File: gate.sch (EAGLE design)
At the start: 0 parts

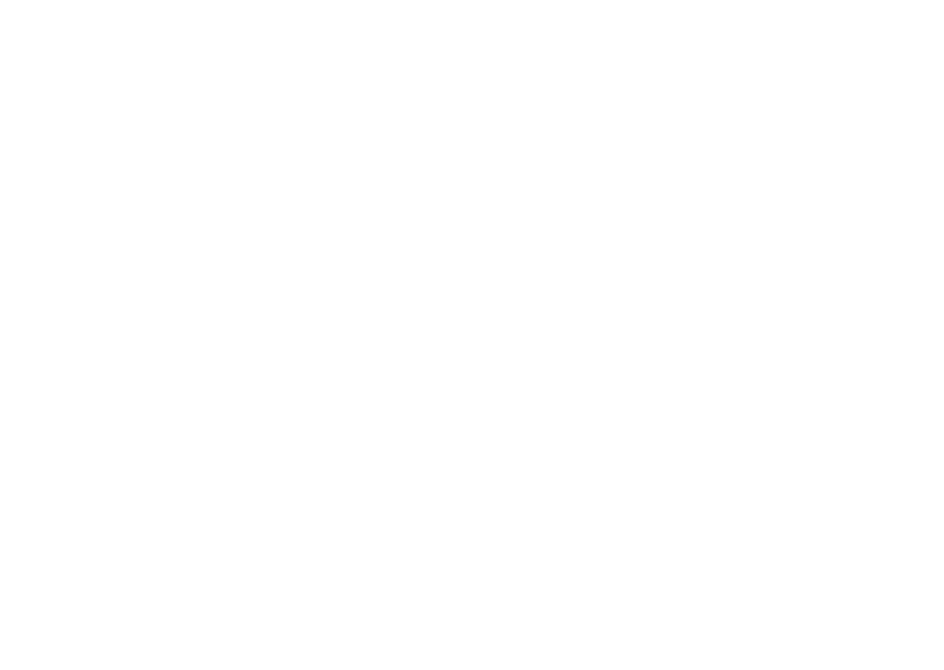
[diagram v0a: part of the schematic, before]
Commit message: Add RS-232 interface
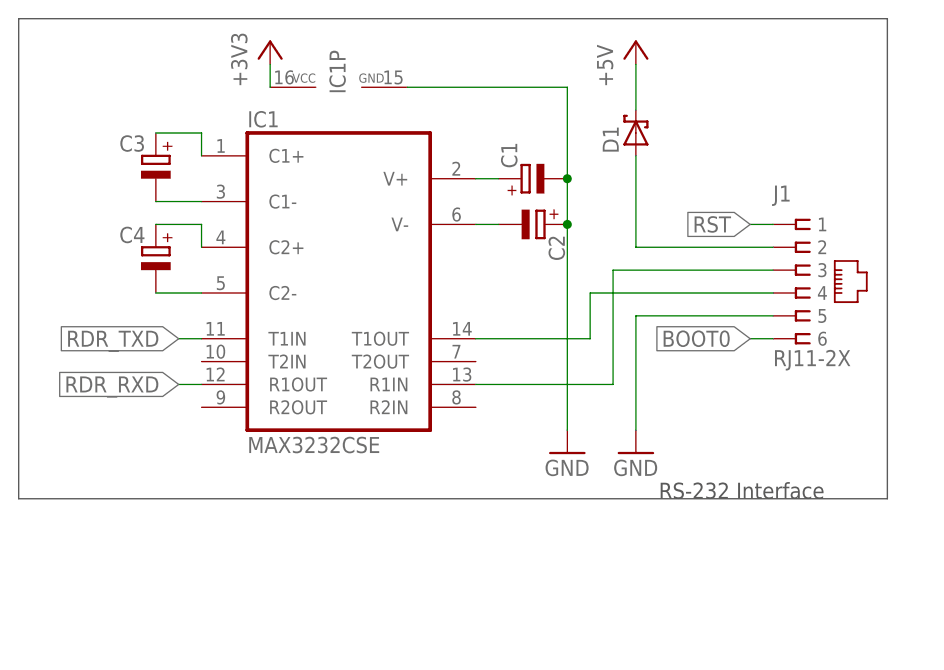
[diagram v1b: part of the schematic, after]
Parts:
- added C1, C2, C3, C4: (no value), rcl:CPOL-EU153CLV-0505
- added D1: (no value), diode:SCHOTTKY-DIODESMD
- added IC1: MAX3232CSE, maxim:MAX3232CSE
- added J1: RJ11-2X, con-tycoelectronics:RJ11-2X
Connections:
- new net +3V3: IC1P.VCC
- new net +5V: D1.C
- new net BOOT0: J1.6
- new net GND: C1.-, C2.+, IC1P.GND, J1.5
- new net N$1: IC1G$1.R1IN, J1.3
- new net N$2: IC1G$1.T1OUT, J1.4
- new net N$3: C3.+, IC1G$1.C1+
- new net N$4: C3.-, IC1G$1.C1-
- new net N$5: C4.+, IC1G$1.C2+
- new net N$6: C4.-, IC1G$1.C2-
- new net N$7: C1.+, IC1G$1.V+
- new net N$8: C2.-, IC1G$1.V-
- new net N$9: D1.A, J1.2
- new net RDR_RXD: IC1G$1.R1OUT
- new net RDR_TXD: IC1G$1.T1IN
- new net RST: J1.1
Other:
- note added: "RS-232 Interface"

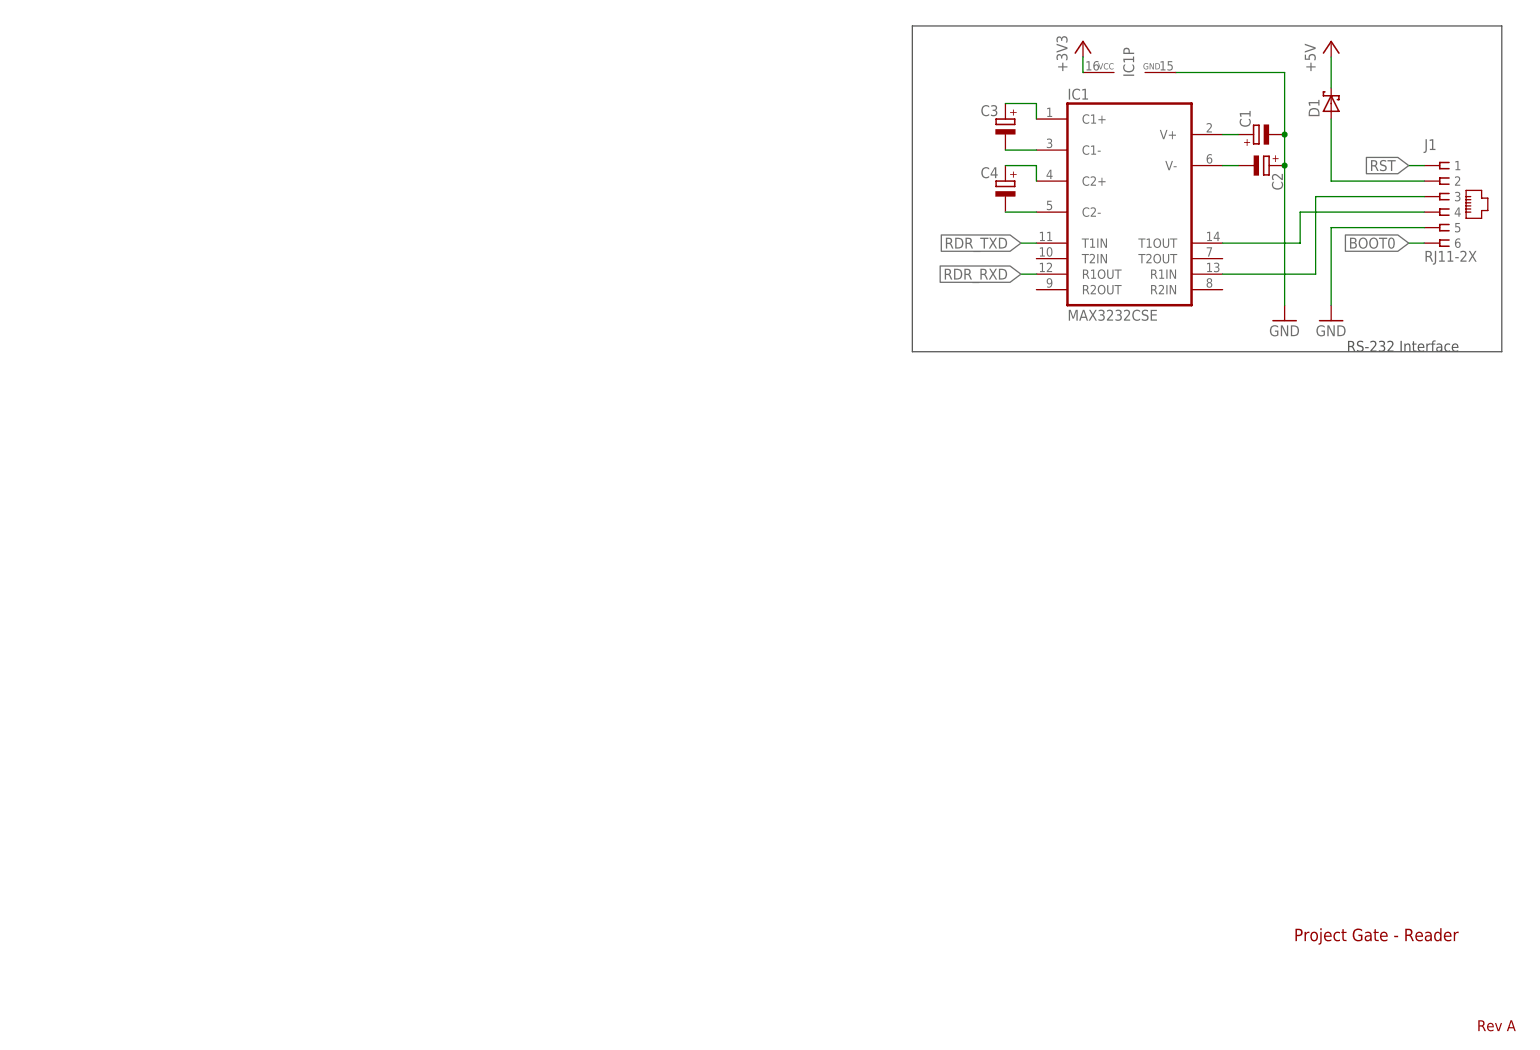
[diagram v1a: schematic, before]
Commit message: Add audio output
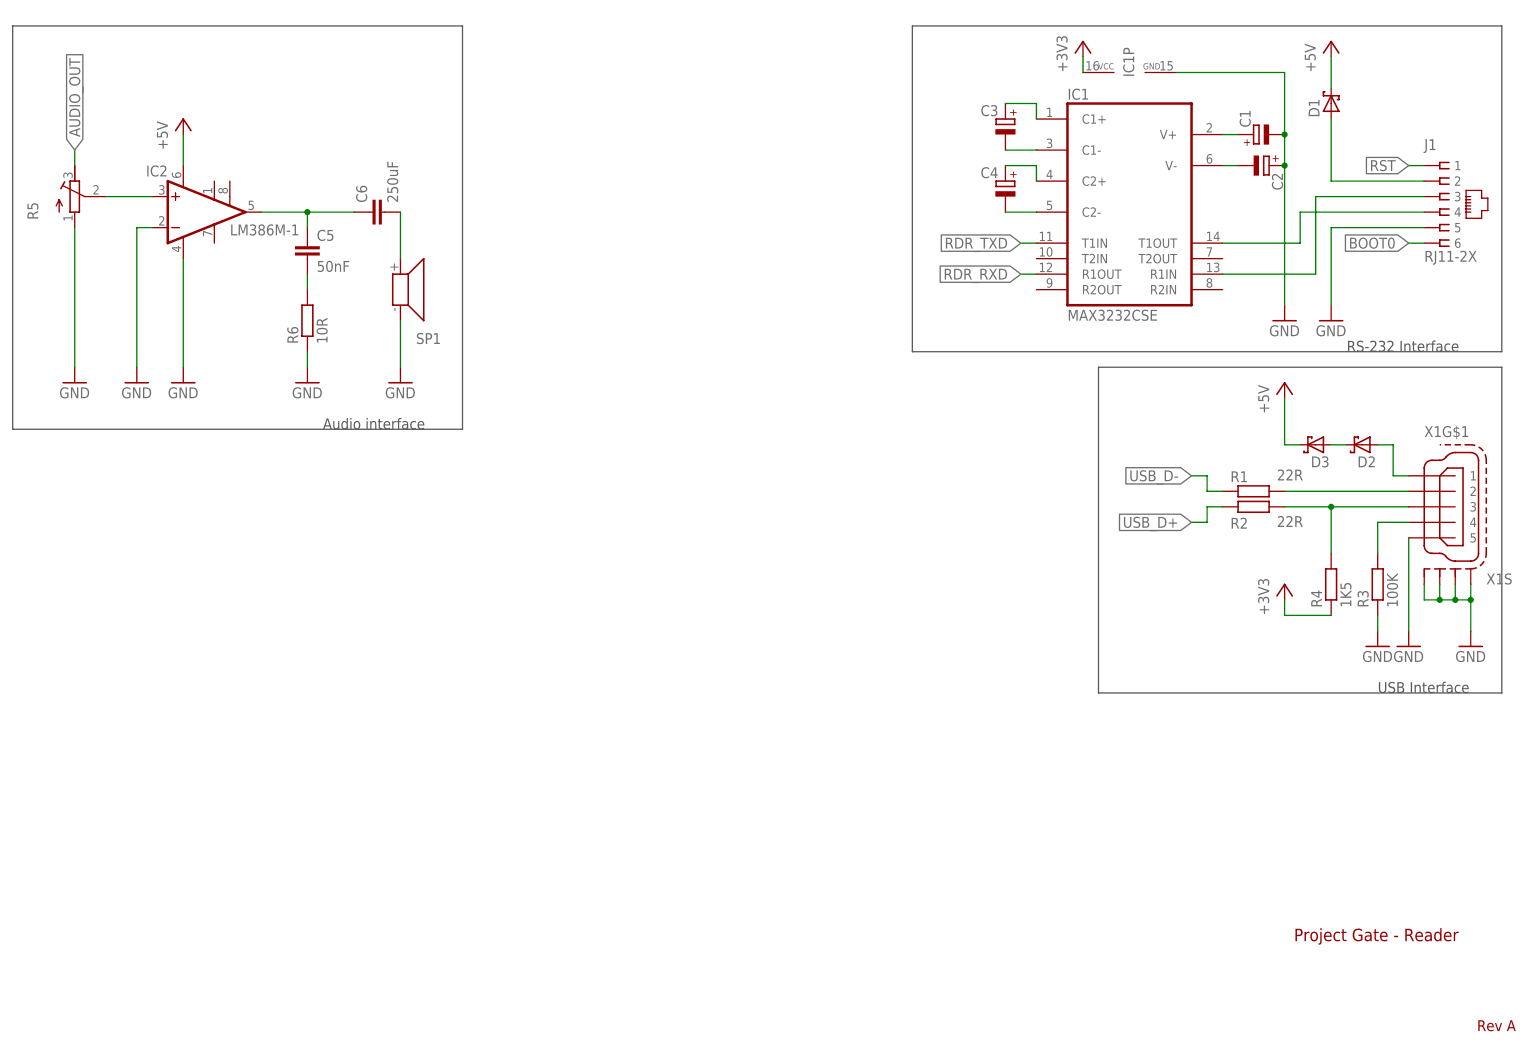
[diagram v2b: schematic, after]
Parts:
- added C5: 50nF, rcl:C-EUC0805
- added C6: 250uF, rcl:C-EUC0805
- added D2, D3: (no value), diode:SCHOTTKY-DIODESMD
- added IC2: LM386M-1, linear:LM386M-1
- added R1, R2: 22R, rcl:R-EU_R0805
- added R3: 100K, rcl:R-EU_R0805
- added R4: 1K5, rcl:R-EU_R0805
- added R5: (no value), rcl:R-TRIMM3339P
- added R6: 10R, rcl:R-EU_R0805
- added SP1: SMS-1308MS-2-R, speaker:SMS-1308MS-2-R
- added X1: MINI-USB-SCHIELD-32005-301, con-cypressindustries:MINI-USB-SCHIELD-32005-301
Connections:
- new net AUDIO_OUT: R5.E
- new net N$10: D2.C, D3.A
- new net N$11: D2.A, X1G$1.1
- new net N$12: R1.2, X1G$1.2
- new net N$13: R2.2, R4.2, X1G$1.3
- new net N$14: R3.2, X1G$1.4
- new net N$15: IC2.+IN, R5.S
- new net N$16: C5.1, C6.1, IC2.OUT
- new net N$17: C5.2, R6.2
- new net N$18: C6.2, SP1.1
- new net USB_D+: R2.1
- new net USB_D-: R1.1
- net +3V3: now also R4.1
- net +5V: now also D3.C, IC2.VS
- net GND: now also IC2.-IN, IC2.GND, R3.1, R5.A, R6.1, SP1.2, X1G$1.5, X1S.S1, X1S.S2, X1S.S3, X1S.S4
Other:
- note added: "Audio interface"
- note added: "USB Interface"

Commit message: Minor mid-review fixes
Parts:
- removed D3: (no value), diode:SCHOTTKY-DIODESMD
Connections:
- removed net N$10: D2.C, D3.A
- new net +12V: D1.C
- net +3V3: now also C1.-
- net +5V: now also D2.C; no longer D1.C, D3.C
- net GND: no longer C1.-
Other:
- moved on the sheet: C1, C2, C3, C4, D1, D2, IC1, IC1P, J1, R1, R2, R3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

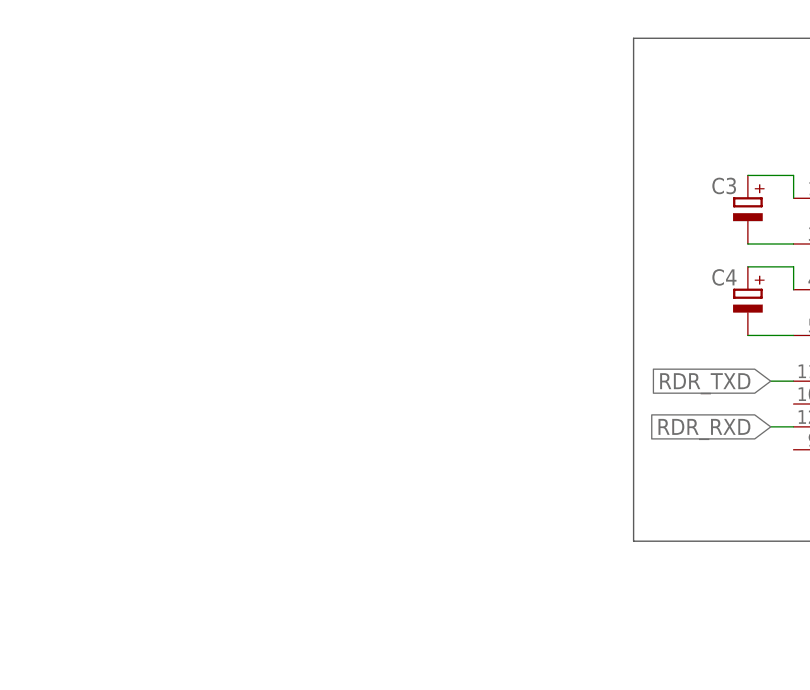
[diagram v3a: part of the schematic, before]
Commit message: Add LEDs
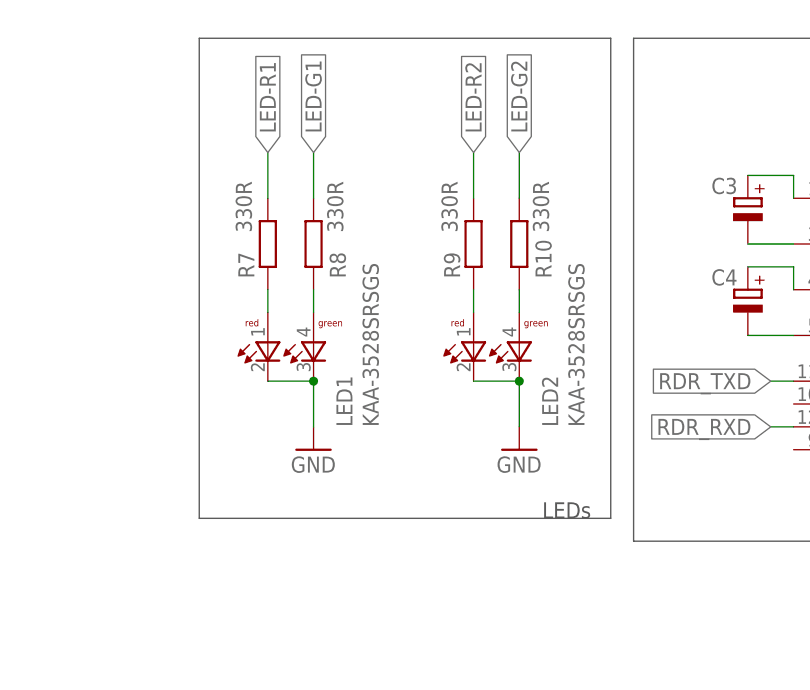
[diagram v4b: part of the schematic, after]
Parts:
- added LED1, LED2: KAA-3528SRSGS, kaa-3528:KAA-3528SRSGS
- added R10, R7, R8, R9: 330R, rcl:R-EU_R0805
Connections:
- new net LED-G1: R8.2
- new net LED-G2: R10.2
- new net LED-R1: R7.2
- new net LED-R2: R9.2
- new net N$10: LED2.A-RED, R9.1
- new net N$19: LED1.A-RED, R7.1
- new net N$20: LED1.A-GREEN, R8.1
- new net N$21: LED2.A-GREEN, R10.1
- net GND: now also LED1.C-GREEN, LED1.C-RED, LED2.C-GREEN, LED2.C-RED
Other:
- note added: "LEDs"
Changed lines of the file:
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@@
 <setting verticaltext="up"/>
 </settings>
-<grid distance="0.1" unitdist="inch" unit="inch" style="lines" multiple="1" display="no" altdistance="0.01" altunitdist="inch" altunit="inch"/>
+<grid distance="0.1" unitdist="inch" unit="inch" style="lines" multiple="1" display="yes" altdistance="0.01" altunitdist="inch" altunit="inch"/>
 <layers>
 <layer number="1" name="Top" color="4" fill="1" visible="no" active="no"/>
@@
 <part name="GND10" library="supply1" deviceset="GND" device=""/>
 <part name="P+1" library="supply1" deviceset="+12V" device=""/>
+<part name="LED1" library="kaa-3528" deviceset="KAA-3528SRSGS" device=""/>
+<part name="GND11" library="supply1" deviceset="GND" device=""/>
+<part name="R7" library="rcl" deviceset="R-EU_" device="R0805" value="330R"/>
+<part name="R8" library="rcl" deviceset="R-EU_" device="R0805" value="330R"/>
+<part name="LED2" library="kaa-3528" deviceset="KAA-3528SRSGS" device=""/>
+<part name="GND12" library="supply1" deviceset="GND" device=""/>
+<part name="R9" library="rcl" deviceset="R-EU_" device="R0805" value="330R"/>
+<part name="R10" library="rcl" deviceset="R-EU_" device="R0805" value="330R"/>
 </parts>
 <sheets>
@@
 <wire x1="7.62" y1="104.14" x2="7.62" y2="170.18" width="0.1524" layer="97"/>
 <text x="58.42" y="104.14" size="1.778" layer="97" font="vector">Audio interface</text>
+<wire x1="106.68" y1="170.18" x2="152.4" y2="170.18" width="0.1524" layer="97"/>
+<wire x1="152.4" y1="170.18" x2="152.4" y2="116.84" width="0.1524" layer="97"/>
+<wire x1="152.4" y1="116.84" x2="106.68" y2="116.84" width="0.1524" layer="97"/>
+<wire x1="106.68" y1="116.84" x2="106.68" y2="170.18" width="0.1524" layer="97"/>
+<text x="144.78" y="116.84" size="1.778" layer="97" font="vector">LEDs</text>
 </plain>
 <instances>
@@
 <instance part="GND10" gate="1" x="71.12" y="111.76"/>
 <instance part="P+1" gate="1" x="223.52" y="165.1"/>
+<instance part="LED1" gate="G$1" x="119.38" y="137.16" smashed="yes">
+<attribute name="NAME" x="123.698" y="127" size="1.778" layer="95" rot="R90"/>
+<attribute name="VALUE" x="126.619" y="127" size="1.778" layer="96" rot="R90"/>
+</instance>
+<instance part="GND11" gate="1" x="119.38" y="124.46"/>
+<instance part="R7" gate="G$1" x="114.3" y="147.32" smashed="yes" rot="R90">
+<attribute name="NAME" x="112.8014" y="143.51" size="1.778" layer="95" rot="R90"/>
+<attribute name="VALUE" x="112.522" y="148.59" size="1.778" layer="96" rot="R90"/>
+</instance>
+<instance part="R8" gate="G$1" x="119.38" y="147.32" smashed="yes" rot="R90">
+<attribute name="NAME" x="122.9614" y="143.51" size="1.778" layer="95" rot="R90"/>
+<attribute name="VALUE" x="122.682" y="148.59" size="1.778" layer="96" rot="R90"/>
+</instance>
+<instance part="LED2" gate="G$1" x="142.24" y="137.16" smashed="yes">
+<attribute name="NAME" x="146.558" y="127" size="1.778" layer="95" rot="R90"/>
+<attribute name="VALUE" x="149.479" y="127" size="1.778" layer="96" rot="R90"/>
+</instance>
+<instance part="GND12" gate="1" x="142.24" y="124.46"/>
+<instance part="R9" gate="G$1" x="137.16" y="147.32" smashed="yes" rot="R90">
+<attribute name="NAME" x="135.6614" y="143.51" size="1.778" layer="95" rot="R90"/>
+<attribute name="VALUE" x="135.382" y="148.59" size="1.778" layer="96" rot="R90"/>
+</instance>
+<instance part="R10" gate="G$1" x="142.24" y="147.32" smashed="yes" rot="R90">
+<attribute name="NAME" x="145.8214" y="143.51" size="1.778" layer="95" rot="R90"/>
+<attribute name="VALUE" x="145.542" y="148.59" size="1.778" layer="96" rot="R90"/>
+</instance>
 </instances>
 <busses>
@@
 <junction x="215.9" y="144.78"/>
 </segment>
+<segment>
+<pinref part="LED1" gate="G$1" pin="C-RED"/>
+<pinref part="LED1" gate="G$1" pin="C-GREEN"/>
+<wire x1="114.3" y1="132.08" x2="119.38" y2="132.08" width="0.1524" layer="91"/>
+<pinref part="GND11" gate="1" pin="GND"/>
+<wire x1="119.38" y1="132.08" x2="119.38" y2="127" width="0.1524" layer="91"/>
+<junction x="119.38" y="132.08"/>
+</segment>
+<segment>
+<pinref part="LED2" gate="G$1" pin="C-RED"/>
+<pinref part="LED2" gate="G$1" pin="C-GREEN"/>
+<wire x1="137.16" y1="132.08" x2="142.24" y2="132.08" width="0.1524" layer="91"/>
+<pinref part="GND12" gate="1" pin="GND"/>
+<wire x1="142.24" y1="132.08" x2="142.24" y2="127" width="0.1524" layer="91"/>
+<junction x="142.24" y="132.08"/>
+</segment>
 </net>
 <net name="N$1" class="0">
@@
 </segment>
 </net>
+<net name="N$19" class="0">
+<segment>
+<pinref part="R7" gate="G$1" pin="1"/>
+<pinref part="LED1" gate="G$1" pin="A-RED"/>
+<wire x1="114.3" y1="142.24" x2="114.3" y2="139.7" width="0.1524" layer="91"/>
+</segment>
+</net>
+<net name="N$20" class="0">
+<segment>
+<pinref part="R8" gate="G$1" pin="1"/>
+<pinref part="LED1" gate="G$1" pin="A-GREEN"/>
+<wire x1="119.38" y1="142.24" x2="119.38" y2="139.7" width="0.1524" layer="91"/>
+</segment>
+</net>
+<net name="N$10" class="0">
+<segment>
+<pinref part="R9" gate="G$1" pin="1"/>
+<pinref part="LED2" gate="G$1" pin="A-RED"/>
+<wire x1="137.16" y1="142.24" x2="137.16" y2="139.7" width="0.1524" layer="91"/>
+</segment>
+</net>
+<net name="N$21" class="0">
+<segment>
+<pinref part="R10" gate="G$1" pin="1"/>
+<pinref part="LED2" gate="G$1" pin="A-GREEN"/>
+<wire x1="142.24" y1="142.24" x2="142.24" y2="139.7" width="0.1524" layer="91"/>
+</segment>
+</net>
+<net name="LED-R1" class="0">
+<segment>
+<pinref part="R7" gate="G$1" pin="2"/>
+<wire x1="114.3" y1="152.4" x2="114.3" y2="157.48" width="0.1524" layer="91"/>
+<label x="114.3" y="157.48" size="1.778" layer="95" rot="R90" xref="yes"/>
+</segment>
+</net>
+<net name="LED-G1" class="0">
+<segment>
+<pinref part="R8" gate="G$1" pin="2"/>
+<wire x1="119.38" y1="152.4" x2="119.38" y2="157.48" width="0.1524" layer="91"/>
+<label x="119.38" y="157.48" size="1.778" layer="95" rot="R90" xref="yes"/>
+</segment>
+</net>
+<net name="LED-R2" class="0">
+<segment>
+<pinref part="R9" gate="G$1" pin="2"/>
+<wire x1="137.16" y1="152.4" x2="137.16" y2="157.48" width="0.1524" layer="91"/>
+<label x="137.16" y="157.48" size="1.778" layer="95" rot="R90" xref="yes"/>
+</segment>
+</net>
+<net name="LED-G2" class="0">
+<segment>
+<pinref part="R10" gate="G$1" pin="2"/>
+<wire x1="142.24" y1="152.4" x2="142.24" y2="157.48" width="0.1524" layer="91"/>
+<label x="142.24" y="157.48" size="1.778" layer="95" rot="R90" xref="yes"/>
+</segment>
+</net>
